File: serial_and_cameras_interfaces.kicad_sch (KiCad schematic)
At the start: 60 parts, among them J13 533980471, J15 533980471, J16 533980471, J17 533980471, J2 WE_68715014522, U16 NTS0102GT, U17 NTS0104PW,118, U18 MAX485EESA, U5 NTS0102GT, U6 PCA9547BS

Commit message: Introduce component standardization
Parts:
- C162, C163: footprint sc606-baseboard-footprints:0402-cap -> sc606-baseboard-footprints:C_0402_1005Metric; Author (none) -> Antmicro; License (none) -> Apache-2.0
- C164, C165, C166, C167, C168, C169, C173, C174, C43, C45: footprint sc606-baseboard-footprints:0402-cap -> sc606-baseboard-footprints:C_0402_1005Metric; Author (none) -> Antmicro; Dielectric (none) -> X5R; License (none) -> Apache-2.0; Voltage (none) -> 50V
- C44: footprint sc606-baseboard-footprints:0402-cap -> sc606-baseboard-footprints:C_0402_1005Metric; Author (none) -> Antmicro; Dielectric (none) -> X5R; License (none) -> Apache-2.0; MPN 0402X104K6R3CT -> GRM155R61H104KE14D; Manufacturer Walsin -> Murata; Voltage (none) -> 50V
- D39, D40: footprint sc606-baseboard-footprints:PUSB3F96X -> sc606-baseboard-footprints:Nexperia_DFN-10_2.5x1mm_P0.5mm; Author (none) -> Antmicro; License (none) -> Apache-2.0
- J13, J15, J16, J17: value 533980471 -> PinHeader_PicoBlade_1x4_P1.25mm_SMD; symbol sc606-baseboard:533980471 -> sc606-baseboard:PinHeader_PicoBlade_1x4_P1.25mm_SMD; Author (none) -> Antmicro; License (none) -> Apache-2.0
- J2: value WE_68715014522 -> Conn_FFC_WE_68715014522_TWO-SIDES; footprint sc606-baseboard-footprints:WE_68715014522 -> sc606-baseboard-footprints:Conn_FFC_WE_68715014x22_ALT; symbol sc606-baseboard:WE_68715014522 -> sc606-baseboard:Conn_FFC_WE_68715014522_TWO-SIDES; Author (none) -> Antmicro; License (none) -> Apache-2.0; MPN 68715014522 -> 68715014522; Manufacturer Wurth Elektronik -> Würth Elektronik
- R1, R175, R176, R177, R180, R185, R33, R34, R35, R36, R37, R45, R46, R47, R48: footprint sc606-baseboard-footprints:0402-res -> sc606-baseboard-footprints:R_0402_1005Metric; Author (none) -> Antmicro; License (none) -> Apache-2.0; MPN CRCW04022K00FKED -> CR0402-FX-2001GLF; Manufacturer VISHAY -> Bourns; Tolerance (none) -> 1%
- R178, R179, R181, R182, R183, R184: footprint sc606-baseboard-footprints:0402-res -> sc606-baseboard-footprints:R_0402_1005Metric; Author (none) -> Antmicro; License (none) -> Apache-2.0; Manufacturer BOURNS -> Bourns; Tolerance (none) -> 1%
- R186, R187, R188, R38, R39, R41, R42, R43, R44: footprint sc606-baseboard-footprints:0402-res -> sc606-baseboard-footprints:R_0402_1005Metric; Author (none) -> Antmicro; Current (none) -> 1A; License (none) -> Apache-2.0; Manufacturer PANASONIC -> Panasonic
- R189: footprint sc606-baseboard-footprints:0603-res -> sc606-baseboard-footprints:R_0603_1608Metric; Author (none) -> Antmicro; License (none) -> Apache-2.0; MPN CRCW0603120RFKEA -> CR0603-FX-1200ELF; Manufacturer VISHAY -> Bourns; Tolerance (none) -> 1%
- R40: footprint sc606-baseboard-footprints:0402-res -> sc606-baseboard-footprints:R_0402_1005Metric; Author (none) -> Antmicro; License (none) -> Apache-2.0; MPN CRCW040210K0FKEDHP -> CR0402-FX-1002GLF; Manufacturer VISHAY -> Bourns; Tolerance (none) -> 1%
- TP64, TP65, TP66: value TP_SMD_1_5MM -> TP_1.5mm_SMD; footprint sc606-baseboard-footprints:TP-R-1.5 -> sc606-baseboard-footprints:TP_SMD_1.5mm; symbol sc606-baseboard:TP_SMD_0_75MM -> sc606-baseboard:TP_1.5mm_SMD; Author (none) -> Antmicro; License (none) -> Apache-2.0
- U16, U5: value NTS0102GT -> NTS0102_XSON; footprint sc606-baseboard-footprints:PSON50P100X195X50-8N -> sc606-baseboard-footprints:XSON-8_1x1.95mm_P0.5mm; symbol sc606-baseboard:NTS0102GT -> sc606-baseboard:NTS0102_XSON; Author (none) -> Antmicro; License (none) -> Apache-2.0; Manufacturer NXP Semiconductors -> NXP
- U17: footprint sc606-baseboard-footprints:TSSOP-14_W4.4mm -> sc606-baseboard-footprints:TSSOP-14_4.4x5mm_P0.65mm; Author (none) -> Antmicro; License (none) -> Apache-2.0; Manufacturer NXP Semiconductors -> NXP
- U18: footprint sc606-baseboard-footprints:SOIC-8_W3.9mm -> sc606-baseboard-footprints:SOIC-8_3.9x4.9x1.75mm_P1.27mm; Author (none) -> Antmicro; License (none) -> Apache-2.0
- U6: value PCA9547BS -> PCA9547_VQFN; footprint sc606-baseboard-footprints:HVQFN24 -> sc606-baseboard-footprints:VQFN-24-1EP_3.8x3.8x1.0mm_P0.5mm; symbol sc606-baseboard:PCA9547BS -> sc606-baseboard:PCA9547_VQFN; Author (none) -> Antmicro; License (none) -> Apache-2.0; Manufacturer NXP -> NXP
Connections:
- no-connect marks 22 -> 32
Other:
- moved on the sheet: C162, C163, C164, C165, C166, C167, C168, C169, C173, C174, C43, C44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

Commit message: [#61796] Run globlib
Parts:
- C162, C163: footprint sc606-baseboard-footprints:C_0402_1005Metric -> antmicro-footprints:C_0402_1005Metric; symbol sc606-baseboard:C_1u_0402 -> antmicroCapacitors0402:C_1u_0402
- C164, C165, C166, C167, C168, C169, C173, C174, C43, C44, C45: footprint sc606-baseboard-footprints:C_0402_1005Metric -> antmicro-footprints:C_0402_1005Metric; symbol sc606-baseboard:C_100n_0402 -> antmicroCapacitors0402:C_100n_0402
- D39, D40: footprint sc606-baseboard-footprints:Nexperia_DFN-10_2.5x1mm_P0.5mm -> antmicro-footprints:Nexperia_DFN-10_2.5x1mm_P0.5mm; symbol sc606-baseboard:PUSB3F96X_PASS -> antmicroTVSDiodes:PUSB3F96X_PASS
- J13, J15, J16, J17: footprint sc606-baseboard-footprints:Molex_PicoBlade_53398-0471_1x04-1MP_P1.25mm_Vertical -> antmicro-footprints:Conn_Molex_PicoBlade_1x4_0533980471; symbol sc606-baseboard:PinHeader_PicoBlade_1x4_P1.25mm_SMD -> antmicroWire2BoardConnectors:Molex_PicoBlade_1x4_0533980471
- R1, R175, R176, R177, R180, R185, R33, R34, R35, R36, R37, R45, R46, R47, R48: footprint sc606-baseboard-footprints:R_0402_1005Metric -> antmicro-footprints:R_0402_1005Metric; symbol sc606-baseboard:R_2k_0402 -> antmicroResistors0402:R_2k_0402
- R178, R179, R181, R182, R183, R184: footprint sc606-baseboard-footprints:R_0402_1005Metric -> antmicro-footprints:R_0402_1005Metric; symbol sc606-baseboard:R_100R_0402 -> antmicroResistors0402:R_100R_0402
- R186, R187, R188, R38, R39, R41, R42, R43, R44: footprint sc606-baseboard-footprints:R_0402_1005Metric -> antmicro-footprints:R_0402_1005Metric; symbol sc606-baseboard:R_0R_0402 -> antmicroResistors0402:R_0R_0402
- R189: footprint sc606-baseboard-footprints:R_0603_1608Metric -> antmicro-footprints:R_0603_1608Metric; symbol sc606-baseboard:R_120R_0603 -> antmicroResistors0603:R_120R_0603
- R40: footprint sc606-baseboard-footprints:R_0402_1005Metric -> antmicro-footprints:R_0402_1005Metric; symbol sc606-baseboard:R_10k_0402 -> antmicroResistors0402:R_10k_0402
- TP64, TP65, TP66: footprint sc606-baseboard-footprints:TP_SMD_1.5mm -> antmicro-footprints:TP_SMD_1.5mm; symbol sc606-baseboard:TP_1.5mm_SMD -> antmicroTestPoints:TP_1.5mm_SMD
- U16, U5: footprint sc606-baseboard-footprints:XSON-8_1x1.95mm_P0.5mm -> antmicro-footprints:XSON-8_1x1.95mm_P0.5mm; symbol sc606-baseboard:NTS0102_XSON -> antmicroLogicTranslatorsLevelShifters:NTS0102_XSON
- U17: footprint sc606-baseboard-footprints:TSSOP-14_4.4x5mm_P0.65mm -> antmicro-footprints:TSSOP-14_4.4x5mm_P0.65mm; symbol sc606-baseboard:NTS0104PW,118 -> antmicroLogicTranslatorsLevelShifters:NTS0104PW,118
- U18: footprint sc606-baseboard-footprints:SOIC-8_3.9x4.9x1.75mm_P1.27mm -> antmicro-footprints:SOIC-8_3.9x4.9x1.75mm_P1.27mm; symbol sc606-baseboard:MAX485EESA -> antmicroInterfaceDriversReceiversTransceivers:MAX485EESA
- U6: footprint sc606-baseboard-footprints:VQFN-24-1EP_3.8x3.8x1.0mm_P0.5mm -> antmicro-footprints:VQFN-24-1EP_3.8x3.8x1.0mm_P0.5mm; symbol sc606-baseboard:PCA9547_VQFN -> antmicroLogicSignalSwitchesMultiplexersDecoders:PCA9547_VQFN

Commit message: [#61796] Update schematics
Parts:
- J13, J15, J16, J17: value PinHeader_PicoBlade_1x4_P1.25mm_SMD -> Molex_PicoBlade_1x4_0533980471
- R186, R188: now not fitted; now left out of the parts list
- U18: Manufacturer Maxim Integrated -> Maxim Integrated Products
- U6: MPN PCA9547BS,118 -> PCA9547BS,118
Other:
- company: (none) -> Antmicro Ltd
- moved on the sheet: C169

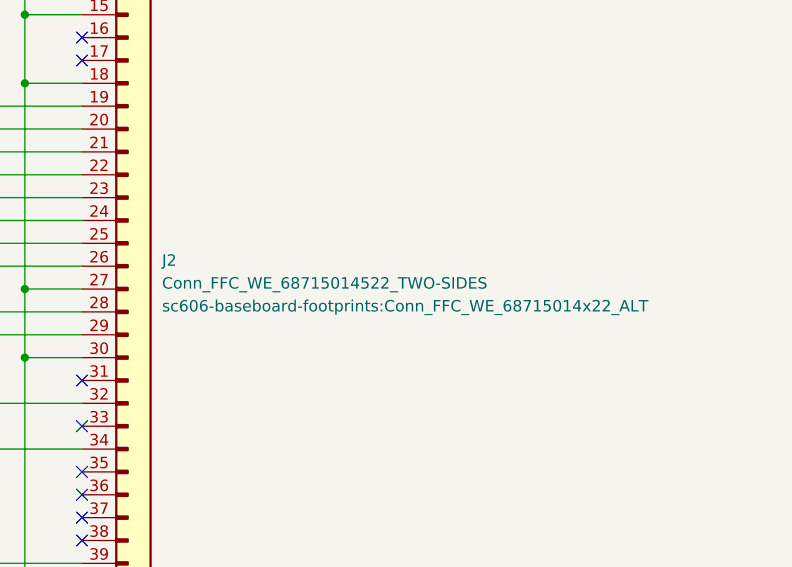
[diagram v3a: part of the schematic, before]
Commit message: [#61796] Clean ERC
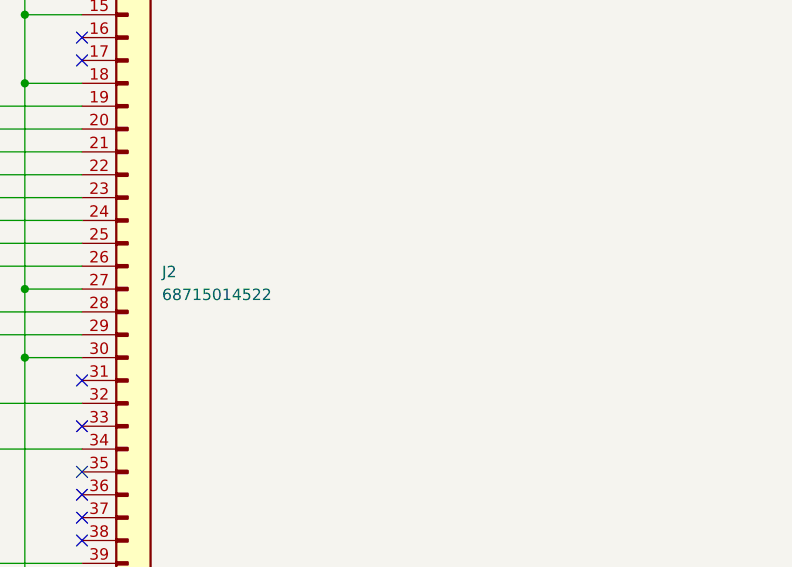
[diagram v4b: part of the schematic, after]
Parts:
- J2: value Conn_FFC_WE_68715014522_TWO-SIDES -> Conn_FFC_WE_68715014522_CUSTOM_TWO-SIDES; footprint sc606-baseboard-footprints:Conn_FFC_WE_68715014x22_ALT -> antmicro-footprints:Conn_FFC_WE_68715014x22_ALT; symbol sc606-baseboard:Conn_FFC_WE_68715014522_TWO-SIDES -> antmicroFCCConnectors:Conn_FFC_WE_68715014522_CUSTOM_TWO-SIDES
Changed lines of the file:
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@@
     )
   )
-  (symbol (lib_id "sc606-baseboard:Conn_FFC_WE_68715014522_TWO-SIDES") (at 374.65 41.91 0) (unit 1)
+  (symbol (lib_id "antmicroFCCConnectors:Conn_FFC_WE_68715014522_CUSTOM_TWO-SIDES") (at 374.65 41.91 0) (unit 1)
     (in_bom yes) (on_board yes) (dnp no) (fields_autoplaced)
-    (property "Reference" "J2" (at 383.54 104.775 0)
+    (property "Reference" "J2" (at 383.54 106.045 0)
       (effects (font (size 1.27 1.27) (thickness 0.15)) (justify left))
     )
-    (property "Value" "Conn_FFC_WE_68715014522_TWO-SIDES" (at 383.54 107.315 0)
+    (property "Value" "Conn_FFC_WE_68715014522_CUSTOM_TWO-SIDES" (at 393.7 46.99 0)
+      (effects (font (size 1.27 1.27) (thickness 0.15)) (justify left bottom) hide)
+    )
+    (property "Footprint" "antmicro-footprints:Conn_FFC_WE_68715014x22_ALT" (at 393.7 49.53 0)
+      (effects (font (size 1.27 1.27) (thickness 0.15)) (justify left bottom) hide)
+    )
+    (property "Datasheet" "https://www.we-online.com/components/products/datasheet/68715014522.pdf" (at 393.7 52.07 0)
+      (effects (font (size 1.27 1.27) (thickness 0.15)) (justify left bottom) hide)
+    )
+    (property "MPN" "68715014522" (at 383.54 108.585 0)
       (effects (font (size 1.27 1.27) (thickness 0.15)) (justify left))
     )
-    (property "Footprint" "sc606-baseboard-footprints:Conn_FFC_WE_68715014x22_ALT" (at 383.54 109.855 0)
-      (effects (font (size 1.27 1.27) (thickness 0.15)) (justify left))
-    )
-    (property "Datasheet" "https://www.we-online.com/components/products/datasheet/68715014522.pdf" (at 393.7 54.61 0)
+    (property "Manufacturer" "Würth Elektronik" (at 393.7 57.15 0)
       (effects (font (size 1.27 1.27) (thickness 0.15)) (justify left bottom) hide)
     )
-    (property "MPN" "68715014522" (at 393.7 57.15 0)
+    (property "Author" "Antmicro" (at 393.7 59.69 0)
       (effects (font (size 1.27 1.27) (thickness 0.15)) (justify left bottom) hide)
     )
-    (property "Manufacturer" "Würth Elektronik" (at 393.7 59.69 0)
+    (property "License" "Apache-2.0" (at 393.7 62.23 0)
       (effects (font (size 1.27 1.27) (thickness 0.15)) (justify left bottom) hide)
     )
-    (property "Author" "Antmicro" (at 393.7 62.23 0)
-      (effects (font (size 1.27 1.27) (thickness 0.15)) (justify left bottom) hide)
-    )
-    (property "License" "Apache-2.0" (at 393.7 64.77 0)
-      (effects (font (size 1.27 1.27) (thickness 0.15)) (justify left bottom) hide)
-    )
